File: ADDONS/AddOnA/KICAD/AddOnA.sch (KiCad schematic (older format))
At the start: 58 parts, among them IC1 FIN1002, IC101 74HC251, IC5 IC_NCP1117LPST33, IC6 PCA9536D, P1 10K0, SW1 Switch_DPDT, SW2 Switch_DPDT, X1 RCA, X101 XLR3, X110 PLR135_T10, X114 CON_IDC26, X115 CON_IDC26, X2 XLR3, X3 RCA, X4 Conn_01x03, X5 MicroMatch14, X6 HDR_02x08, X7 PLT133_T10W, X8 CON_USB_B, X9 USB_A

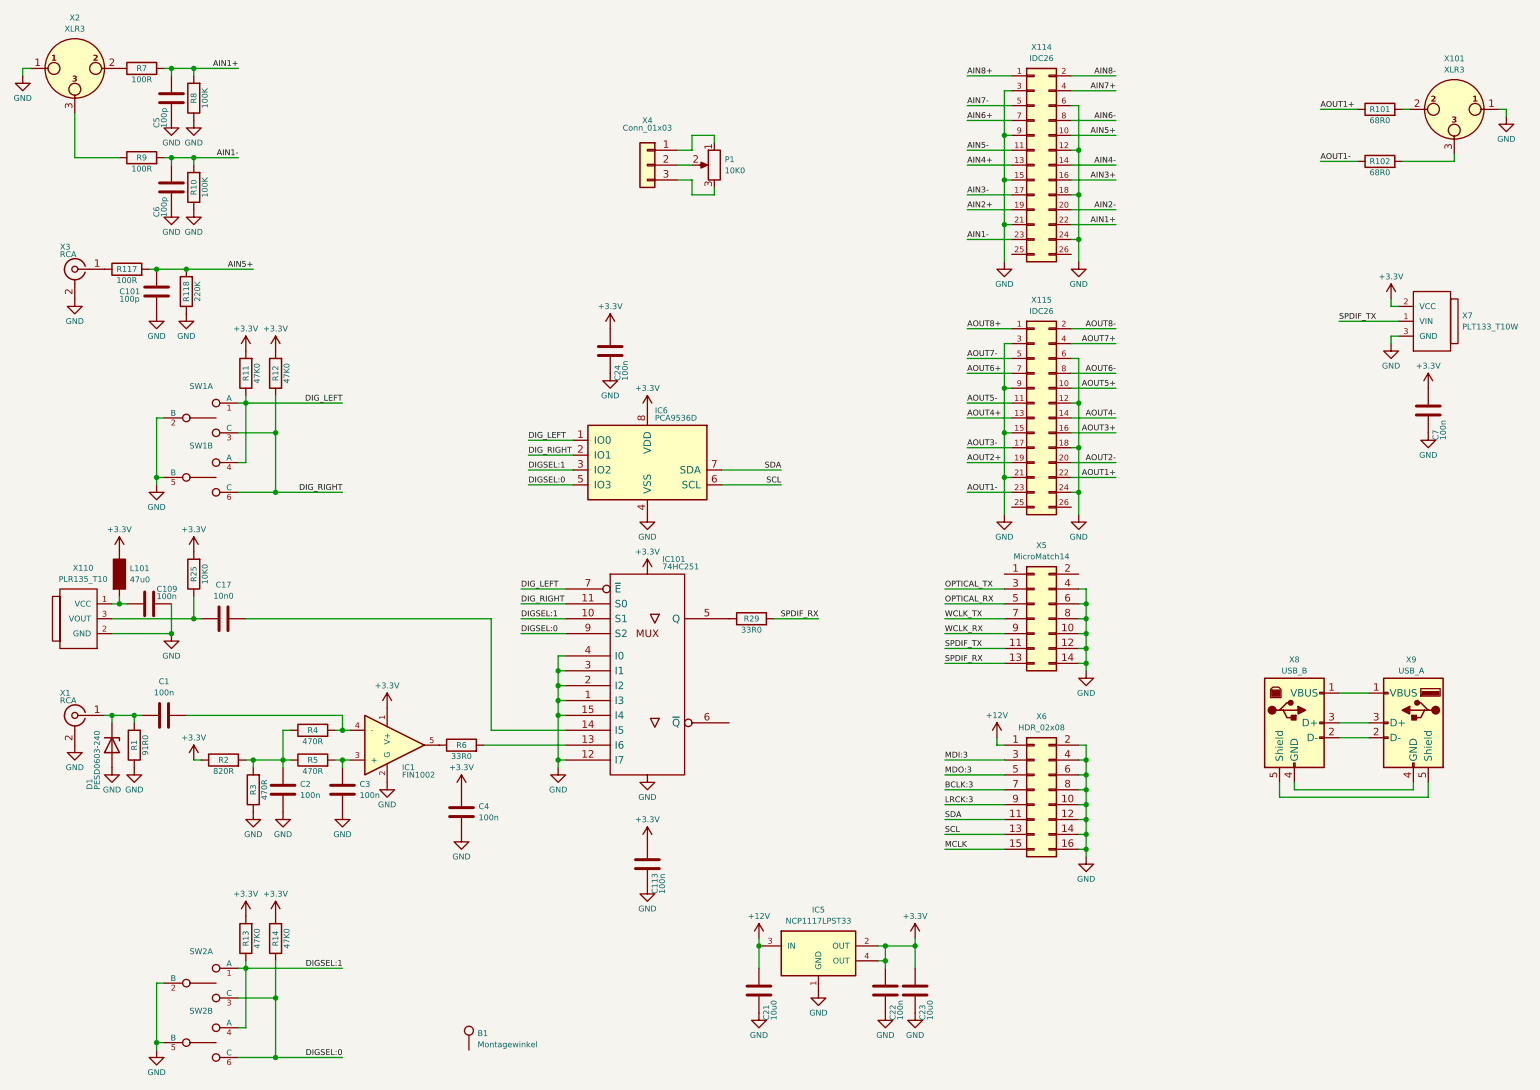
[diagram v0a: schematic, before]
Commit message: Added USB-A connector
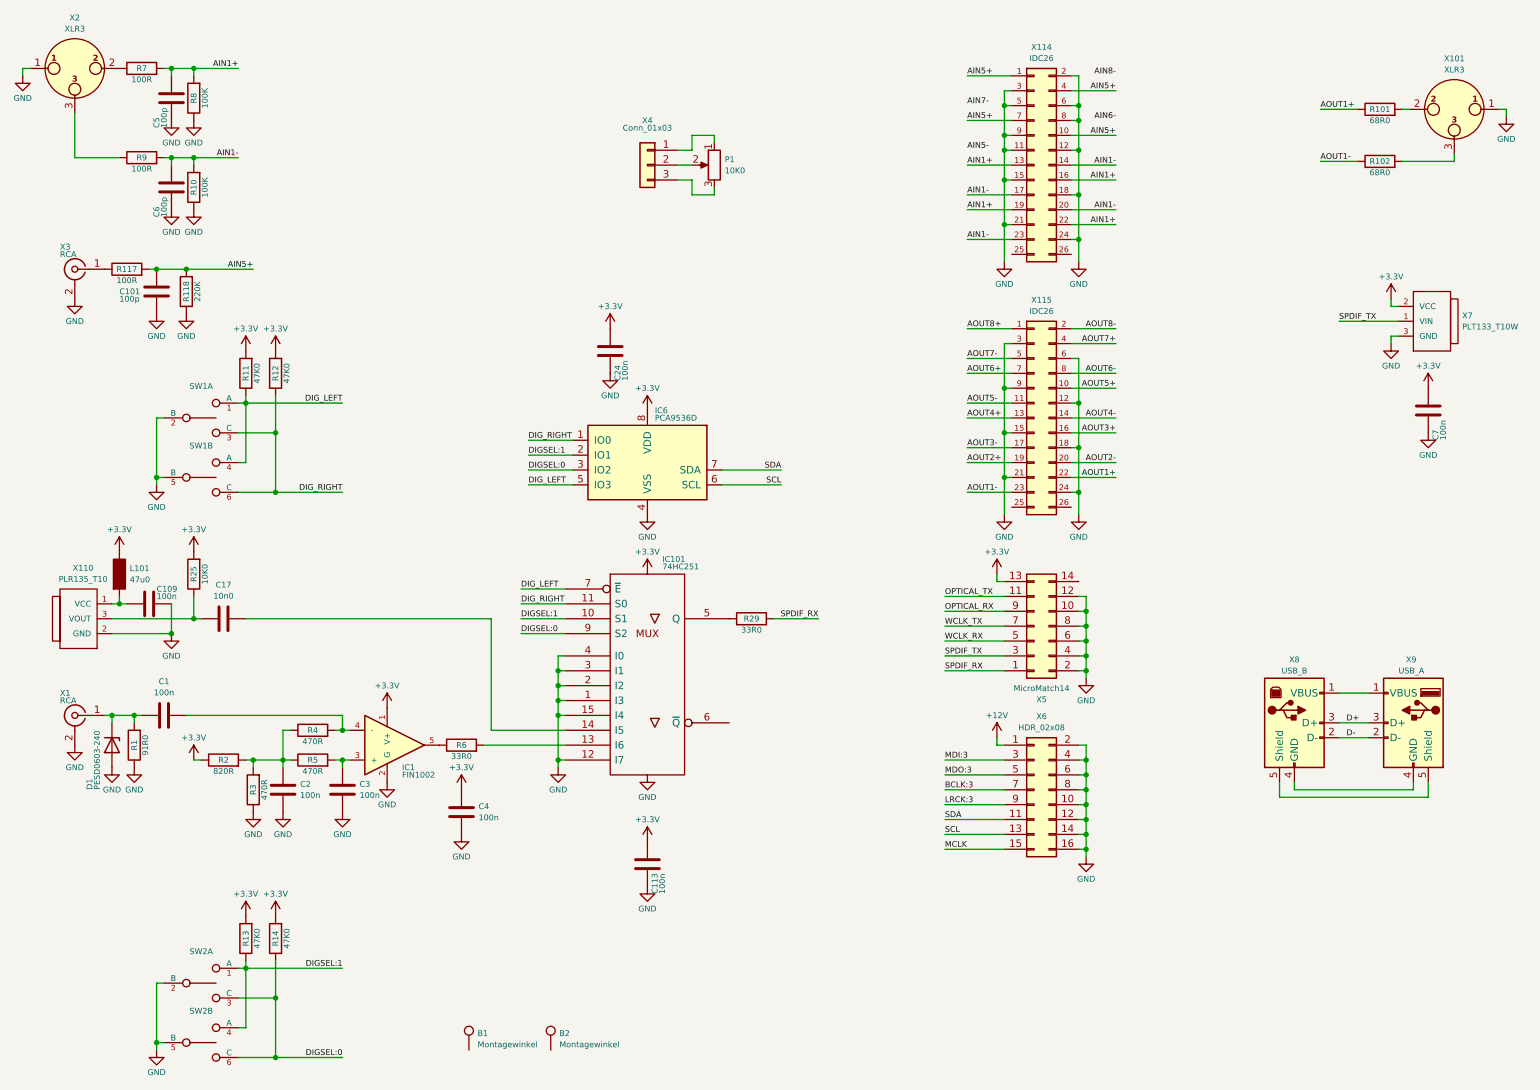
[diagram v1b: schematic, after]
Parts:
- removed C21, C23: CAP_10u0_25V_X5R_0805, rklib:C0805-X7R, symbol rk:CAP_10u0_25V_X5R_0805
- removed C22: CAP_100n_50V_X7R_0805, rklib:C0805-X7R, symbol rk:CAP_100n_50V_X7R_0805
- removed IC5: IC_NCP1117LPST33, rklib:SOT223, symbol rk:IC_NCP1117LPST33
- added B2: Montagewinkel, rklib:Montagewinkel, symbol Connector:TestPoint
- X7: footprint (none) -> rklib:PLT133_T10W
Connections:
- net AIN2+ is gone; now on net AIN1+: X114.19 (Pin_19)
- net AIN2- is gone; now on net AIN1-: X114.20 (Pin_20)
- net AIN3+ is gone; now on net AIN1+: X114.16 (Pin_16)
- net AIN3- is gone; now on net AIN1-: X114.17 (Pin_17)
- net AIN4+ is gone; now on net AIN1+: X114.13 (Pin_13)
- net AIN4- is gone; now on net AIN1-: X114.14 (Pin_14)
- net AIN6+ is gone; now on net AIN5+: X114.7 (Pin_7)
- net AIN7+ is gone; now on net AIN5+: X114.4 (Pin_4)
- net AIN8+ is gone; now on net AIN5+: X114.1 (Pin_1)
- net +3V3: now also X5.13 (Pin_13)
- net AIN5-: no longer X114.11 (Pin_11)
- net AIN6-: no longer X114.8 (Pin_8)
- net AIN7-: no longer X114.5 (Pin_5)
- net AIN8-: no longer X114.2 (Pin_2)
- net DIGSEL:0: now also IC6.3 (IO2); no longer IC6.5 (IO3)
- net DIGSEL:1: now also IC6.2 (IO1); no longer IC6.3 (IO2)
- net DIG_LEFT: now also IC6.5 (IO3); no longer IC6.1 (IO0)
- net DIG_RIGHT: now also IC6.1 (IO0); no longer IC6.2 (IO1)
- net GND: now also X114.11 (Pin_11), X114.2 (Pin_2), X114.5 (Pin_5), X114.8 (Pin_8), X5.2 (Pin_2); no longer X5.14 (Pin_14)
- net OPTICAL_RX: now also X5.9 (Pin_9); no longer X5.5 (Pin_5)
- net OPTICAL_TX: now also X5.11 (Pin_11); no longer X5.3 (Pin_3)
- net SPDIF_RX: now also X5.1 (Pin_1); no longer X5.13 (Pin_13)
- net SPDIF_TX: now also X5.3 (Pin_3); no longer X5.11 (Pin_11)
- net WCLK_RX: now also X5.5 (Pin_5); no longer X5.9 (Pin_9)
- net D-: now reaches X8.2 (D-), X9.2 (D-)
- net D+: now reaches X8.3 (D+), X9.3 (D+)
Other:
- moved on the sheet: X5

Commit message: Updated Gerbers
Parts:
- removed X9: USB_A, Connector_USB:USB_A_CNCTech_1001-011-01101_Horizontal, symbol Connector:USB_A
- added X9: HDR_01x05, Connector_PinHeader_2.54mm:PinHeader_1x05_P2.54mm_Vertical, symbol Connector_Generic:Conn_01x05
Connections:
- net +3V3: now also IC101.10 (S1), IC101.11 (S0)
- net D+: now also X9.3 (Pin_3)
- net D-: now also X9.2 (Pin_2)
- net DIGSEL:1: no longer IC101.10 (S1)
- net DIG_LEFT: no longer IC101.7 (~E)
- net DIG_RIGHT: no longer IC101.11 (S0)
- net GND: now also IC101.14 (I5), IC101.7 (~E); no longer IC101.12 (I7)
- net at R6.2: now also IC101.12 (I7); no longer IC101.13 (I6)
- net at C17.2: now also IC101.13 (I6); no longer IC101.14 (I5)
- net at X8.1 (VBUS): now also X9.1 (Pin_1)
- net at X8.4 (GND): now also X9.4 (Pin_4)
- net at X8.5 (Shield): now also X9.5 (Pin_5)
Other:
- moved on the sheet: C24, IC101, IC6, R29

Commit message: Updated BOM for AddOnA
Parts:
- C1, C101, C109, C113, C2, C24, C3, C4, C7: Manufacturer KEMET -> Kemet
- P1: Manufacturer (none) -> Alps; pn (none) -> RK09K1110A0J
- R10, R8: Manufacturer (none) -> Yageo
- R11, R12, R13, R14: Manufacturer (none) -> Yageo; pn (none) -> RC0805FR-0747KL
- R7, R9: Manufacturer (none) -> Stackpole Electronics Inc
- SW1, SW2: Manufacturer (none) -> TE Connectivity Alcoswitch; pn (none) -> A203MD9AB04
- X2: Manufacturer (none) -> Neutrik; pn (none) -> NC3FAH1
- X4: Manufacturer (none) -> Molex; pn (none) -> 0530470310
- X7: Manufacturer (none) -> Everlight Electronics Co Ltd; pn (none) -> PLT133/T10W
- X8: Manufacturer (none) -> On Shore Technology Inc.; pn (none) -> USB-B1HSB6
- X9: Manufacturer (none) -> Sullins Connector Solutions; pn (none) -> PRPC005SAAN-RC
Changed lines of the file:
@@
 F 5 "5% 50V C0G/NP0" H 1500 2200 39  0001 C CNN "Value2"
 F 6 "399-1122-1-ND" H 1500 2150 39  0001 C CNN "digikey"
-F 7 "KEMET" H -1050 1100 50  0001 C CNN "Manufacturer"
+F 7 "Kemet" H -1050 1100 50  0001 C CNN "Manufacturer"
 F 8 "C0805C101J5GACTU" H -1050 1100 50  0001 C CNN "pn"
 	1    1500 2450
@@
 F 5 "5% 50V X7R" H 1450 4300 39  0001 C CNN "Value2"
 F 6 "399-1170-1-ND" H 1450 4250 39  0001 C CNN "digikey"
-F 7 "KEMET" H -3550 3000 50  0001 C CNN "Manufacturer"
+F 7 "Kemet" H -3550 3000 50  0001 C CNN "Manufacturer"
 F 8 "C0805C104K5RACTU" H -3550 3000 50  0001 C CNN "pn"
 	1    1450 4550
@@
 F 5 "5% 50V X7R" H 4800 6050 39  0001 C CNN "Value2"
 F 6 "399-1170-1-ND" H 4800 6000 39  0001 C CNN "digikey"
-F 7 "KEMET" H -3450 450 50  0001 C CNN "Manufacturer"
+F 7 "Kemet" H -3450 450 50  0001 C CNN "Manufacturer"
 F 8 "C0805C104K5RACTU" H -3450 450 50  0001 C CNN "pn"
 	1    4800 6300
@@
 F 5 "5% 50V X7R" H 1550 5050 39  0001 C CNN "Value2"
 F 6 "399-1170-1-ND" H 1550 5000 39  0001 C CNN "digikey"
-F 7 "KEMET" H -3550 650 50  0001 C CNN "Manufacturer"
+F 7 "Kemet" H -3550 650 50  0001 C CNN "Manufacturer"
 F 8 "C0805C104K5RACTU" H -3550 650 50  0001 C CNN "pn"
 	1    1550 5300
@@
 F 5 "5% 50V X7R" H 3550 5700 39  0001 C CNN "Value2"
 F 6 "399-1170-1-ND" H 3550 5650 39  0001 C CNN "digikey"
-F 7 "KEMET" H -3550 650 50  0001 C CNN "Manufacturer"
+F 7 "Kemet" H -3550 650 50  0001 C CNN "Manufacturer"
 F 8 "C0805C104K5RACTU" H -3550 650 50  0001 C CNN "pn"
 	1    3550 5950
@@
 F 5 "5% 50V X7R" H 2750 5550 39  0001 C CNN "Value2"
 F 6 "399-1170-1-ND" H 2750 5500 39  0001 C CNN "digikey"
-F 7 "KEMET" H -3550 650 50  0001 C CNN "Manufacturer"
+F 7 "Kemet" H -3550 650 50  0001 C CNN "Manufacturer"
 F 8 "C0805C104K5RACTU" H -3550 650 50  0001 C CNN "pn"
 	1    2750 5800
@@
 F 5 "5% 50V X7R" H 2350 5550 39  0001 C CNN "Value2"
 F 6 "399-1170-1-ND" H 2350 5500 39  0001 C CNN "digikey"
-F 7 "KEMET" H -3550 650 50  0001 C CNN "Manufacturer"
+F 7 "Kemet" H -3550 650 50  0001 C CNN "Manufacturer"
 F 8 "C0805C104K5RACTU" H -3550 650 50  0001 C CNN "pn"
 	1    2350 5800
@@
 F 5 "5% 50V X7R" H 4550 2000 39  0001 C CNN "Value2"
 F 6 "399-1170-1-ND" H 4550 1950 39  0001 C CNN "digikey"
-F 7 "KEMET" H -3450 -100 50  0001 C CNN "Manufacturer"
+F 7 "Kemet" H -3450 -100 50  0001 C CNN "Manufacturer"
 F 8 "C0805C104K5RACTU" H -3450 -100 50  0001 C CNN "pn"
 	1    4550 2250
@@
 F 6 "RNCP0805FTD100RCT-ND" H 1400 650 39  0001 C CNN "digikey"
 F 7 "RNCP0805FTD100R" H -2500 -100 50  0001 C CNN "pn"
+F 8 "Stackpole Electronics Inc" H 0   0   50  0001 C CNN "Manufacturer"
 	1    1400 950
 	1    0    0    -1
@@
 F 6 "311-100KCRCT-ND" H 1750 850 39  0001 C CNN "digikey"
 F 7 "RC0805FR-07100KL" H -2500 -100 50  0001 C CNN "pn"
+F 8 "Yageo" H 0   0   50  0001 C CNN "Manufacturer"
 	1    1750 1150
 	0    -1   -1   0
@@
 F 6 "RNCP0805FTD100RCT-ND" H 1400 1250 39  0001 C CNN "digikey"
 F 7 "RNCP0805FTD100R" H -2500 -100 50  0001 C CNN "pn"
+F 8 "Stackpole Electronics Inc" H 0   0   50  0001 C CNN "Manufacturer"
 	1    1400 1550
 	1    0    0    -1
@@
 F 6 "311-100KCRCT-ND" H 1750 1450 39  0001 C CNN "digikey"
 F 7 "RC0805FR-07100KL" H -2500 -100 50  0001 C CNN "pn"
+F 8 "Yageo" H 0   0   50  0001 C CNN "Manufacturer"
 	1    1750 1750
 	0    -1   -1   0
@@
 F 2 "rklib:NC3FAH" H 950 950 50  0001 C CNN
 F 3 " ~" H 950 950 50  0001 C CNN
+F 4 "Neutrik" H 0   0   50  0001 C CNN "Manufacturer"
+F 5 "NC3FAH1" H 0   0   50  0001 C CNN "pn"
 	1    950  950
 	1    0    0    -1
@@
 F 5 "1% 0.125W Thick" H 2100 2875 39  0001 C CNN "Value2"
 F 6 "311-47.0KCRCT-ND" H 2100 2700 39  0001 C CNN "digikey"
+F 7 "Yageo" H 0   0   50  0001 C CNN "Manufacturer"
+F 8 "RC0805FR-0747KL" H 0   0   50  0001 C CNN "pn"
 	1    2100 3000
 	0    -1   -1   0
@@
 F 5 "1% 0.125W Thick" H 2300 2875 39  0001 C CNN "Value2"
 F 6 "311-47.0KCRCT-ND" H 2300 2700 39  0001 C CNN "digikey"
+F 7 "Yageo" H 0   0   50  0001 C CNN "Manufacturer"
+F 8 "RC0805FR-0747KL" H 0   0   50  0001 C CNN "pn"
 	1    2300 3000
 	0    -1   -1   0
@@
 F 2 "rklib:GEMINI_A" H 1800 7100 50  0001 C CNN
 F 3 "" H 1800 7100 50  0000 C CNN
+F 4 "TE Connectivity Alcoswitch " H 0   0   50  0001 C CNN "Manufacturer"
+F 5 "A203MD9AB04" H 0   0   50  0001 C CNN "pn"
 	1    1800 7100
 	1    0    0    -1
@@
 F 2 "rklib:GEMINI_A" H 1800 7500 50  0001 C CNN
 F 3 "" H 1800 7500 50  0000 C CNN
+F 4 "TE Connectivity Alcoswitch " H 0   0   50  0001 C CNN "Manufacturer"
+F 5 "A203MD9AB04" H 0   0   50  0001 C CNN "pn"
 	2    1800 7500
 	1    0    0    -1
@@
 F 5 "1% 0.125W Thick" H 2100 6675 39  0001 C CNN "Value2"
 F 6 "311-47.0KCRCT-ND" H 2100 6500 39  0001 C CNN "digikey"
+F 7 "Yageo" H 0   0   50  0001 C CNN "Manufacturer"
+F 8 "RC0805FR-0747KL" H 0   0   50  0001 C CNN "pn"
 	1    2100 6800
 	0    -1   -1   0
@@
 F 5 "1% 0.125W Thick" H 2300 6675 39  0001 C CNN "Value2"
 F 6 "311-47.0KCRCT-ND" H 2300 6500 39  0001 C CNN "digikey"
+F 7 "Yageo" H 0   0   50  0001 C CNN "Manufacturer"
+F 8 "RC0805FR-0747KL" H 0   0   50  0001 C CNN "pn"
 	1    2300 6800
 	0    -1   -1   0
@@
 F 2 "rklib:GEMINI_A" H 1800 3700 50  0001 C CNN
 F 3 "" H 1800 3700 50  0000 C CNN
+F 4 "TE Connectivity Alcoswitch " H 0   0   50  0001 C CNN "Manufacturer"
+F 5 "A203MD9AB04" H 0   0   50  0001 C CNN "pn"
 	2    1800 3700
 	1    0    0    -1
@@
 F 2 "rklib:GEMINI_A" H 1800 3300 50  0001 C CNN
 F 3 "" H 1800 3300 50  0000 C CNN
+F 4 "TE Connectivity Alcoswitch " H 0   0   50  0001 C CNN "Manufacturer"
+F 5 "A203MD9AB04" H 0   0   50  0001 C CNN "pn"
 	1    1800 3300
 	1    0    0    -1
@@
 F 2 "rklib:PLT133_T10W" H 10450 2650 60  0001 C CNN
 F 3 "" H 10450 2650 60  0000 C CNN
+F 4 "Everlight Electronics Co Ltd" H 0   0   50  0001 C CNN "Manufacturer"
+F 5 "PLT133/T10W" H 0   0   50  0001 C CNN "pn"
 	1    10450 2650
 	-1   0    0    -1
@@
 F 5 "5% 50V X7R" H 10050 3000 39  0001 C CNN "Value2"
 F 6 "399-1170-1-ND" H 10050 2950 39  0001 C CNN "digikey"
-F 7 "KEMET" H 2050 900 50  0001 C CNN "Manufacturer"
+F 7 "Kemet" H 2050 900 50  0001 C CNN "Manufacturer"
 F 8 "C0805C104K5RACTU" H 2050 900 50  0001 C CNN "pn"
 	1    10050 3250
@@
 F 2 "rklib:Molex_PicoBlade_530470310" H 4800 1600 50  0001 C CNN
 F 3 "~" H 4800 1600 50  0001 C CNN
+F 4 "Molex" H 0   0   50  0001 C CNN "Manufacturer"
+F 5 "0530470310" H 0   0   50  0001 C CNN "pn"
 	1    4800 1600
 	-1   0    0    -1
@@
 F 2 "rklib:RK09K1110-20" H 5250 1600 50  0001 C CNN
 F 3 "~" H 5250 1600 50  0001 C CNN
+F 4 "Alps" H 0   0   50  0001 C CNN "Manufacturer"
+F 5 "RK09K1110A0J" H 0   0   50  0001 C CNN "pn"
 	1    5250 1600
 	-1   0    0    -1
@@
 F 5 "horizontal" H 9150 4750 39  0001 C CNN "Value2"
 F 6 "ED2983-ND" H 9150 4700 39  0001 C CNN "digikey"
+F 7 "On Shore Technology Inc." H 0   0   50  0001 C CNN "Manufacturer"
+F 8 "USB-B1HSB6" H 0   0   50  0001 C CNN "pn"
 	1    9150 5350
 	1    0    0    -1
@@
 F 2 "Connector_PinHeader_2.54mm:PinHeader_1x05_P2.54mm_Vertical" H 10100 5350 50  0001 C CNN
 F 3 "~" H 10100 5350 50  0001 C CNN
+F 4 "Sullins Connector Solutions" H 0   0   50  0001 C CNN "Manufacturer"
+F 5 "PRPC005SAAN-RC" H 0   0   50  0001 C CNN "pn"
 	1    10100 5350
 	1    0    0    -1

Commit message: Minor changes on AddOn A
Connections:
- net GND: now also IC101.13 (I6); no longer IC101.1 (I3)
- net at C17.2: now also IC101.1 (I3); no longer IC101.13 (I6)
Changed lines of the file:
@@
 	2100 4650 3750 4650
-Wire Wire Line
-	4250 5100 4200 5100
-Connection ~ 4200 5100
 Wire Wire Line
 	4250 4900 4200 4900
@@
 Wire Wire Line
 	4200 4350 4250 4350
-Wire Wire Line
-	4200 5200 4200 5100
 Connection ~ 4200 5200
 Wire Wire Line
 	4250 5200 4200 5200
 Wire Wire Line
-	3750 4650 3750 5400
-Wire Wire Line
 	4200 5000 4200 4900
-Wire Wire Line
-	4200 5100 4200 5000
 Connection ~ 4200 5000
 Wire Wire Line
@@
 	4250 5500 3700 5500
 Wire Wire Line
-	4250 5400 3750 5400
-Wire Wire Line
 	4250 5300 4200 5300
 Connection ~ 4200 5300
 Wire Wire Line
-	4200 5300 4200 5550
+	4200 5300 4200 5400
+Wire Wire Line
+	4200 5000 4200 5200
+Wire Wire Line
+	4250 5100 3750 5100
+Wire Wire Line
+	3750 5100 3750 4650
+Wire Wire Line
+	4250 5400 4200 5400
+Connection ~ 4200 5400
+Wire Wire Line
+	4200 5400 4200 5550
 $EndSCHEMATC

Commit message: Mechanical redefinition of board edges AddOnA
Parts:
- renumbered B1 to B101, B2 to B102, C5 to C101, C6 to C102, C24 to C103, C101 to C104, C7 to C105, C109 to C106, C17 to C107, C1 to C108, C2 to C109, C3 to C110, C4 to C111, C113 to C112, D1 to D101, IC6 to IC101, IC101 to IC102, IC1 to IC103, P1 to P101, R7 to R101, R8 to R102, R101 to R103, R9 to R104, R102 to R105, R10 to R106, R117 to R107, R118 to R108, R11 to R109, R12 to R110, R25 to R111, R29 to R112, R4 to R113, R1 to R114, R6 to R115, R2 to R116, R5 to R117, R3 to R118, R13 to R119, R14 to R120, SW1 to SW101, SW2 to SW102, X2 to X101, X101 to X102, X4 to X103, X114 to X104, X3 to X105, X7 to X106, X115 to X107, X110 to X108, X5 to X109, X1 to X110, X8 to X111, X9 to X112, X6 to X113

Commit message: Fixed issue #42
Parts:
- IC101: symbol Interface_Expansion:PCA9536D -> AddOnA-rescue:PCA9536D-Interface_Expansion
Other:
- note added: "Select between \nanalog XLR+RCA,\ndigital coax or \ntoslink input"
- note added: "Select left or right\nchannel of digital\ninput"
- moved on the sheet: R109, R110, R119, R120, SW101A, SW101B, SW102A, SW102B
